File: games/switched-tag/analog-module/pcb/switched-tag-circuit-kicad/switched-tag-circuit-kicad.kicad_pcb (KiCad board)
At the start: 2 copper layers, 56 parts, among them Q1 RUL035N02, Q2 RUL035N02, Q3 RUL035N02, U13 TLV9154IDR, U14 TLV9154IDR, U15 TLV9154IDR

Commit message: Saving pcb placement.
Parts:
- removed Q3: RUL035N02, Package_TO_SOT_SMD:SOT-89-5
- removed R39: 1k, Resistor_SMD:R_0603_1608Metric
- moved R38 76.5 mm to (144.9, 91.6), turned to 90 degrees
- moved Q2 74.0 mm to (139.9, 90.6), turned to 90 degrees
- moved R34 68.8 mm to (123.8, 89.3), turned to 90 degrees
- moved D7 68.6 mm to (129.2, 86.0), turned to 0 degrees
- moved D6 63.8 mm to (123.8, 85.3)
- moved R33 63.0 mm to (124.6, 80.5), turned to 180 degrees
- moved R32 62.8 mm to (128.1, 82.5), turned to 0 degrees
- moved R37 61.6 mm to (142.3, 82.6)
- moved R35 60.7 mm to (131.9, 82.4), turned to 0 degrees
- moved R36 55.4 mm to (131.9, 78.6), turned to 180 degrees
- moved Q1 52.9 mm to (140.3, 77.1), turned to 90 degrees
- moved R31 51.2 mm to (120.8, 72.7), turned to -90 degrees
- moved U13 47.1 mm to (128.9, 72.1), turned to -90 degrees
- moved D4 47.0 mm to (77.1, 80.7), turned to -90 degrees
- moved R30 44.9 mm to (137.2, 71.5)
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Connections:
- U14 pad 13: /Switched Tag 2D Collision Detection/U4_V- -> /Switched Tag 2D Collision Detection/U3_V-
- U14 pad 14: /Switched Tag 2D Collision Detection/U4_Vout -> /Switched Tag 2D Collision Detection/U3_Vout
- U14 pad 8: /Switched Tag 2D Collision Detection/U3_Vout -> /Switched Tag 2D Collision Detection/U4_Vout
- U14 pad 9: /Switched Tag 2D Collision Detection/U3_V- -> /Switched Tag 2D Collision Detection/U4_V-
- U15 pad 1: /Switched Tag 2D Collision Detection/U5_Vout -> /Switched Tag 2D Collision Detection/U7_Vout
- U15 pad 10: /Switched Tag 2D Collision Detection/U7_V+ -> GND
- U15 pad 12: /Switched Tag 2D Collision Detection/U8_V+ -> GND
- U15 pad 13: /Switched Tag 2D Collision Detection/U7_Vout -> /Switched Tag 2D Collision Detection/U3_Vout
- U15 pad 14: /Switched Tag 2D Collision Detection/U8_Vout -> /Switched Tag 2D Collision Detection/U5_Vout
- U15 pad 2: /Switched Tag 2D Collision Detection/U3_Vout -> /Switched Tag 2D Collision Detection/U7_V-
- U15 pad 3: GND -> /Switched Tag 2D Collision Detection/U7_V+
- U15 pad 5: GND -> /Switched Tag 2D Collision Detection/U8_V+
- U15 pad 6: /Switched Tag 2D Collision Detection/U4_Vout -> /Switched Tag 2D Collision Detection/U7_Vout
- U15 pad 7: /Switched Tag 2D Collision Detection/U6_Vout -> /Switched Tag 2D Collision Detection/U8_Vout
- U15 pad 8: /Switched Tag 2D Collision Detection/U7_Vout -> /Switched Tag 2D Collision Detection/U6_Vout
- U15 pad 9: /Switched Tag 2D Collision Detection/U7_V- -> /Switched Tag 2D Collision Detection/U4_Vout
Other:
- board outline added: 81.3 x 45.7 mm
- board text added: "+3V3 Zone"
- board text added: "-3V3 Zone"
- board text added: "0"
- board text added: "?"
- board text added: "? mm"
- board text added: "B.Cu"
- board text added: "B.Mask"
- board text added: "B.Paste"
- board text added: "B.Silkscreen"
- board text added: "Bottom Silk Screen"
- board text added: "Bottom Solder Mask"
- board text added: "Bottom Solder Paste"
- board text added: "Color"
- board text added: "Dielectric"
- board text added: "Epsilon R"
- board text added: "F.Cu"
- board text added: "F.Mask"
- board text added: "F.Paste"
- board text added: "F.Silkscreen"
- board text added: "FR4"
- board text added: "Layer Name"
- board text added: "Loss Tangent"
- board text added: "Material"
- board text added: "Not specified"
- board text added: "Origin here."
- board text added: "Thickness (mm)"
- board text added: "Top Silk Screen"
- board text added: "Top Solder Mask"
- board text added: "Top Solder Paste"
- board text added: "Type"
- board text added: "copper"
- board text added: "core"

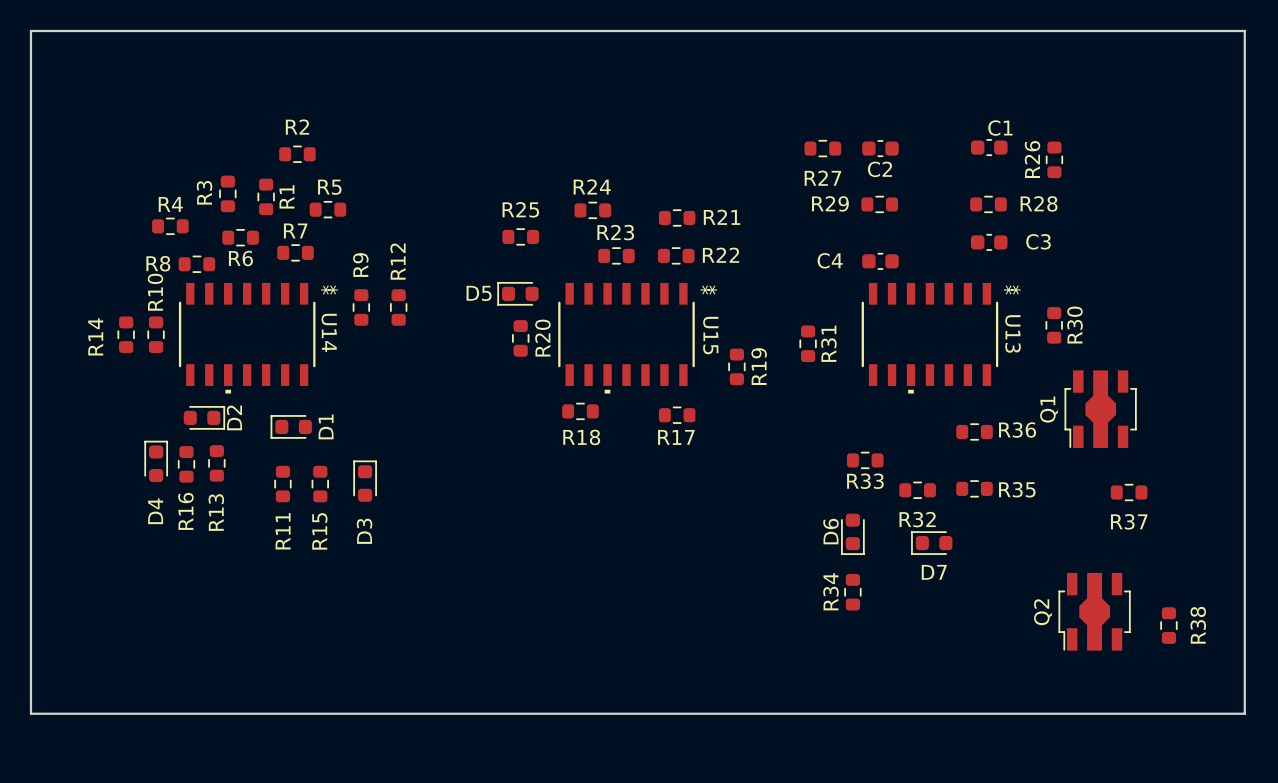
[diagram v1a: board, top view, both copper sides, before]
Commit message: Changed component size from 0603 to 0805 for easier hand soldering.
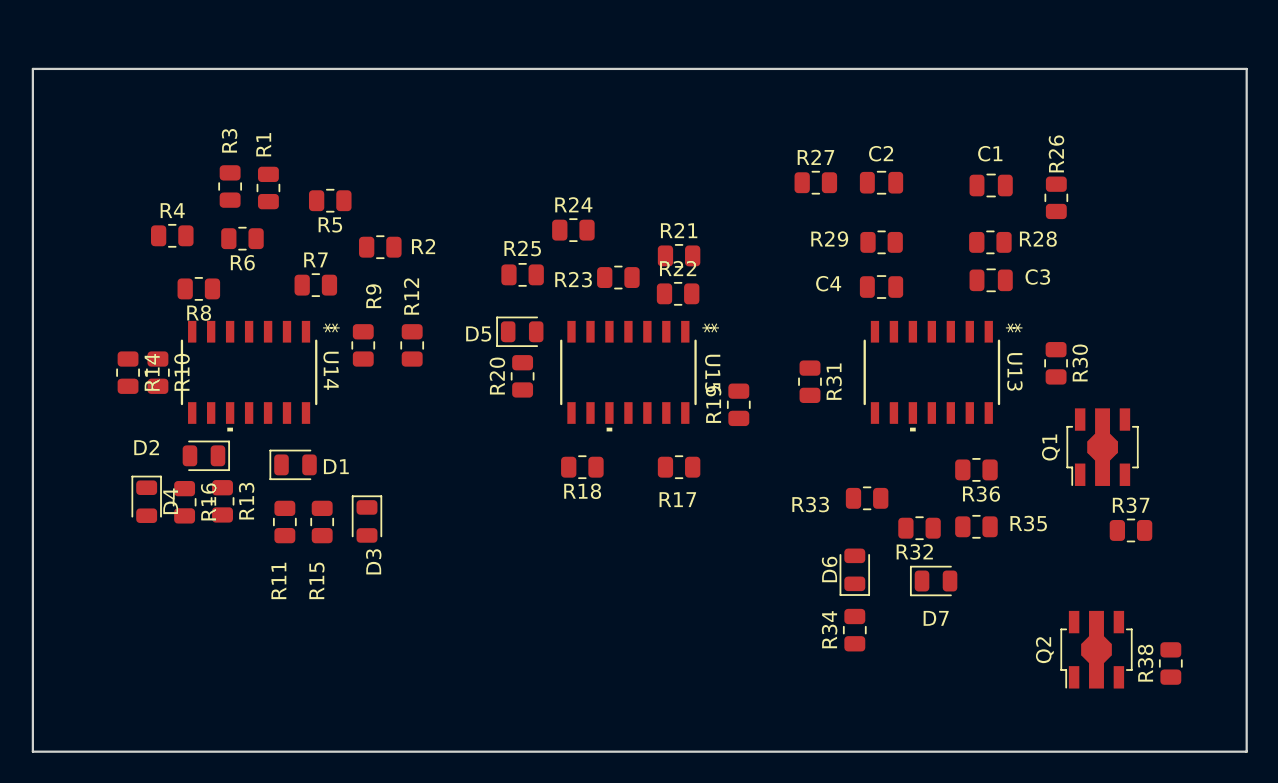
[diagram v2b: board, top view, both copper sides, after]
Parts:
- C1, C2, C3, C4: footprint Capacitor_SMD:C_0603_1608Metric -> Capacitor_SMD:C_0805_2012Metric
- D1, D2, D3, D4, D5, D6, D7: footprint Diode_SMD:D_0603_1608Metric -> Diode_SMD:D_0805_2012Metric
- R1, R10, R11, R12, R13, R14, R15, R16, R17, R18, R19, R2, R20, R21, R22, R23, R24, R25, R26, R27, R28, R29, R3, R30, R31, R32, R33, R34, R35, R36, R37, R38, R4, R5, R6, R7, R8, R9: footprint Resistor_SMD:R_0603_1608Metric -> Resistor_SMD:R_0805_2012Metric
- moved R2 8.34 mm to (92.1, 66.2)
- moved R18 3.74 mm to (105.6, 81.0)
- moved R17 3.48 mm to (112.1, 81.0)
- moved R12 2.70 mm to (94.2, 72.8)
- moved D4 2.62 mm to (76.5, 83.3)
- moved R13 2.57 mm to (81.5, 83.2)
- moved R7 2.55 mm to (87.8, 68.8)
- moved D1 2.54 mm to (86.4, 80.8)
- moved D5 2.54 mm to (101.6, 71.9)
- moved R21 2.54 mm to (112.1, 66.8)
- moved R28 2.54 mm to (133.0, 65.9)
- moved R29 2.54 mm to (125.7, 65.9)
- moved R31 2.54 mm to (120.9, 75.2)
- moved R32 2.54 mm to (128.2, 85.0)
- moved R34 2.54 mm to (123.9, 91.9)
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
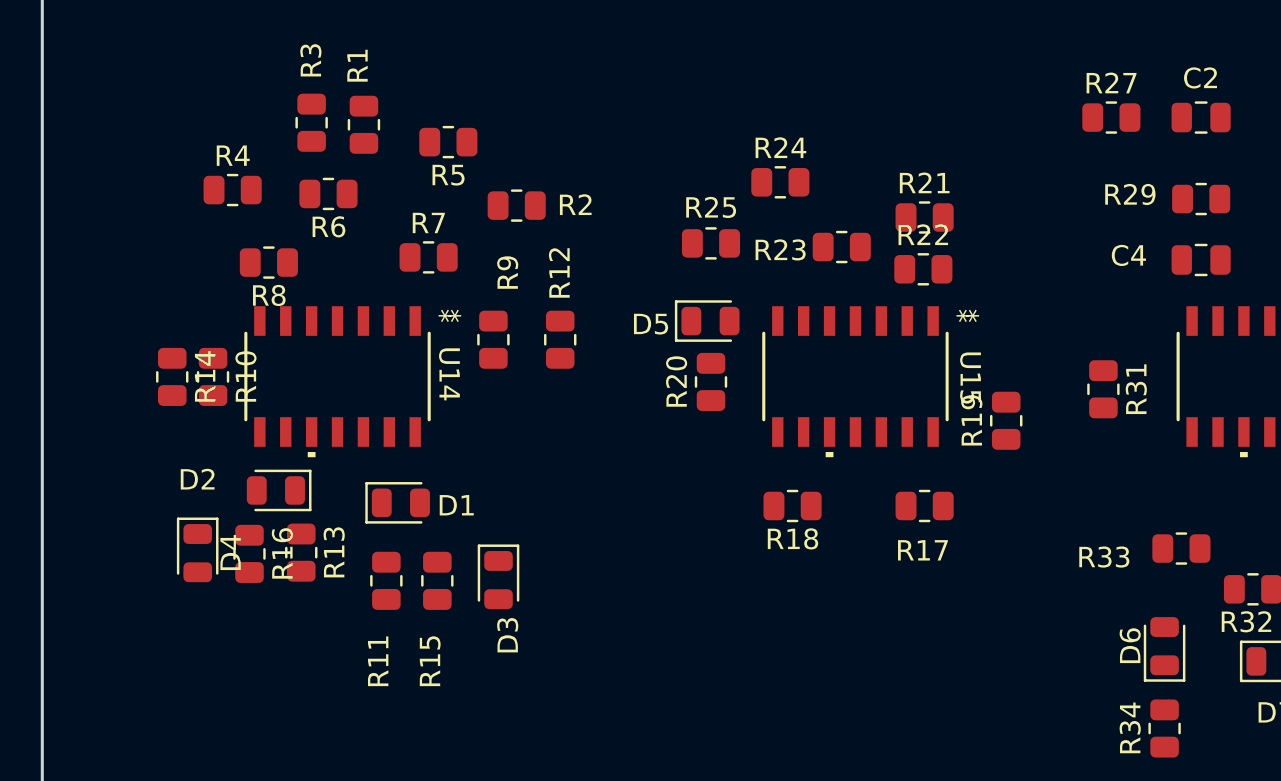
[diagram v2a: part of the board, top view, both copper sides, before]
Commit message: Added new block diagram and general requirements.
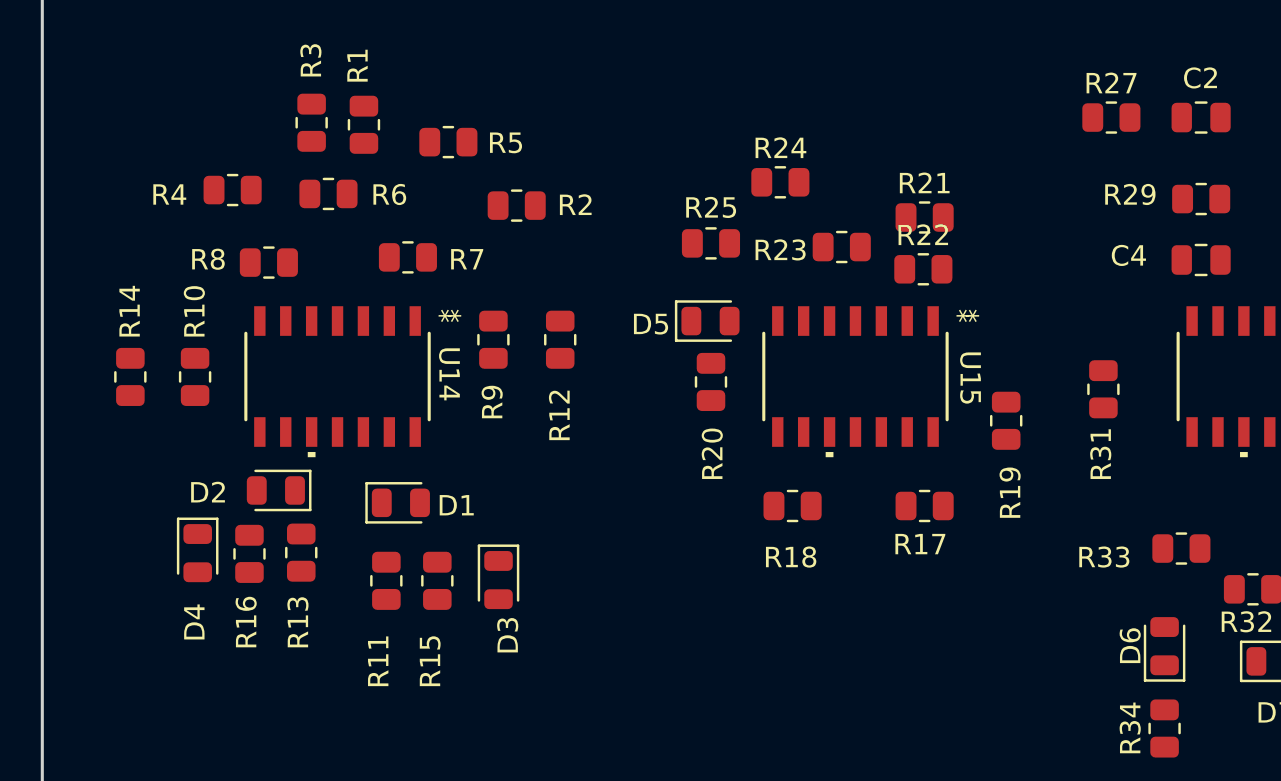
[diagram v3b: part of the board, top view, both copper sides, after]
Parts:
- moved R14 2.05 mm to (73.2, 74.6)
- moved R7 1.02 mm to (86.8, 68.8)
- moved R10 0.88 mm to (76.3, 74.6)
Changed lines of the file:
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@@
     (property "ki_keywords" "diode")
     (attr smd)
-    (fp_text reference "D2" (at 3.8355 0.508 180) (layer "F.SilkS")
+    (fp_text reference "D2" (at 3.3275 -0.127 180) (layer "F.SilkS")
         (effects (font (size 1 1) (thickness 0.15)))
     )
@@
   )
   (footprint "Resistor_SMD:R_0805_2012Metric" (layer "F.Cu")
-    (at 77.22 74.62 -90)
+    (at 76.34 74.62 -90)
     (descr "Resistor SMD 0805 (2012 Metric), square (rectangular) end terminal, IPC_7351 nominal, (Body size source: IPC-SM-782 page 72, https://www.pcb-3d.com/wordpress/wp-content/uploads/ipc-sm-782a_amendment_1_and_2.pdf), generated with kicad-footprint-generator")
     (tags "resistor")
@@
     (property "ki_keywords" "R res resistor")
     (attr smd)
-    (fp_text reference "R10" (at 0 -1.65 -90) (layer "F.SilkS")
+    (fp_text reference "R10" (at -3.195 0 -90) (layer "F.SilkS")
         (effects (font (size 1 1) (thickness 0.15)))
     )
@@
     (property "ki_keywords" "R res resistor")
     (attr smd)
-    (fp_text reference "R5" (at 0 -1.65 180) (layer "F.SilkS")
+    (fp_text reference "R5" (at -2.8194 -0.0649 180) (layer "F.SilkS")
         (effects (font (size 1 1) (thickness 0.15)))
     )
@@
         (effects (font (size 1 1) (thickness 0.15)))
     )
-    (fp_text value "TLV9154IDR" (at 0 6.35 -90 unlocked) (layer "F.Fab")
+    (fp_text value "TLV9154IDR" (at 0 5.08 -90 unlocked) (layer "F.Fab")
         (effects (font (size 1 1) (thickness 0.15)))
     )
@@
     (property "ki_keywords" "R res resistor")
     (attr smd)
-    (fp_text reference "R31" (at 0 -1.65 -90) (layer "F.SilkS")
+    (fp_text reference "R31" (at 3.183652 0.095 -90) (layer "F.SilkS")
         (effects (font (size 1 1) (thickness 0.15)))
     )
@@
     (property "ki_keywords" "R res resistor")
     (attr smd)
-    (fp_text reference "R13" (at 0 -1.65 -90) (layer "F.SilkS")
+    (fp_text reference "R13" (at 3.429 0.127 -90) (layer "F.SilkS")
         (effects (font (size 1 1) (thickness 0.15)))
     )
@@
     (property "ki_keywords" "R res resistor")
     (attr smd)
-    (fp_text reference "R18" (at 0 -1.65 180) (layer "F.SilkS")
+    (fp_text reference "R18" (at 0.091 -2.54 180) (layer "F.SilkS")
         (effects (font (size 1 1) (thickness 0.15)))
     )
@@
     (property "ki_keywords" "diode")
     (attr smd)
-    (fp_text reference "D4" (at 0 -1.65 -90) (layer "F.SilkS")
+    (fp_text reference "D4" (at 3.4035 0.127 -90) (layer "F.SilkS")
         (effects (font (size 1 1) (thickness 0.15)))
     )
@@
   )
   (footprint "Resistor_SMD:R_0805_2012Metric" (layer "F.Cu")
-    (at 87.7935 68.758)
+    (at 86.7775 68.758)
     (descr "Resistor SMD 0805 (2012 Metric), square (rectangular) end terminal, IPC_7351 nominal, (Body size source: IPC-SM-782 page 72, https://www.pcb-3d.com/wordpress/wp-content/uploads/ipc-sm-782a_amendment_1_and_2.pdf), generated with kicad-footprint-generator")
     (tags "resistor")
@@
     (property "ki_keywords" "R res resistor")
     (attr smd)
-    (fp_text reference "R7" (at 0 -1.65) (layer "F.SilkS")
+    (fp_text reference "R7" (at 2.8975 0.127) (layer "F.SilkS")
         (effects (font (size 1 1) (thickness 0.15)))
     )
@@
     (property "ki_keywords" "R res resistor")
     (attr smd)
-    (fp_text reference "R8" (at 0 -1.65 180) (layer "F.SilkS")
+    (fp_text reference "R8" (at 2.984 0.127 180) (layer "F.SilkS")
         (effects (font (size 1 1) (thickness 0.15)))
     )
@@
     (property "ki_keywords" "R res resistor")
     (attr smd)
-    (fp_text reference "R4" (at 0 -1.65) (layer "F.SilkS")
+    (fp_text reference "R4" (at -3.111 0.254) (layer "F.SilkS")
         (effects (font (size 1 1) (thickness 0.15)))
     )
@@
     (property "ki_keywords" "R res resistor")
     (attr smd)
-    (fp_text reference "R6" (at 0 -1.65 180) (layer "F.SilkS")
+    (fp_text reference "R6" (at -2.984 -0.063 180) (layer "F.SilkS")
         (effects (font (size 1 1) (thickness 0.15)))
     )
@@
     (property "ki_keywords" "R res resistor")
     (attr smd)
-    (fp_text reference "R16" (at 0 -1.65 -90) (layer "F.SilkS")
+    (fp_text reference "R16" (at 3.366 0.127 -90) (layer "F.SilkS")
         (effects (font (size 1 1) (thickness 0.15)))
     )
@@
     (property "ki_keywords" "R res resistor")
     (attr smd)
-    (fp_text reference "R9" (at -3.275 -0.737 -90) (layer "F.SilkS")
+    (fp_text reference "R9" (at 3.075 0.025 -90) (layer "F.SilkS")
         (effects (font (size 1 1) (thickness 0.15)))
     )
@@
   )
   (footprint "Resistor_SMD:R_0805_2012Metric" (layer "F.Cu")
-    (at 75.22 74.62 -90)
+    (at 73.165 74.62 -90)
     (descr "Resistor SMD 0805 (2012 Metric), square (rectangular) end terminal, IPC_7351 nominal, (Body size source: IPC-SM-782 page 72, https://www.pcb-3d.com/wordpress/wp-content/uploads/ipc-sm-782a_amendment_1_and_2.pdf), generated with kicad-footprint-generator")
     (tags "resistor")
@@
     (property "ki_keywords" "R res resistor")
     (attr smd)
-    (fp_text reference "R14" (at 0 -1.65 -90) (layer "F.SilkS")
+    (fp_text reference "R14" (at -3.195 0 -90) (layer "F.SilkS")
         (effects (font (size 1 1) (thickness 0.15)))
     )
@@
     (property "ki_keywords" "R res resistor")
     (attr smd)
-    (fp_text reference "R19" (at 0 -1.65 90) (layer "F.SilkS")
+    (fp_text reference "R19" (at -3.544652 0.227 90) (layer "F.SilkS")
         (effects (font (size 1 1) (thickness 0.15)))
     )
@@
     (property "ki_keywords" "R res resistor")
     (attr smd)
-    (fp_text reference "R20" (at 0 -1.65 90) (layer "F.SilkS")
+    (fp_text reference "R20" (at -3.543652 0.1 90) (layer "F.SilkS")
         (effects (font (size 1 1) (thickness 0.15)))
     )
@@
     (property "ki_keywords" "R res resistor")
     (attr smd)
-    (fp_text reference "R17" (at -0.09 2.210652) (layer "F.SilkS")
+    (fp_text reference "R17" (at -0.217 1.905) (layer "F.SilkS")
         (effects (font (size 1 1) (thickness 0.15)))
     )
@@
     (property "ki_keywords" "R res resistor")
     (attr smd)
-    (fp_text reference "R12" (at -3.275 0 -90) (layer "F.SilkS")
+    (fp_text reference "R12" (at 3.71 0 -90) (layer "F.SilkS")
         (effects (font (size 1 1) (thickness 0.15)))
     )
